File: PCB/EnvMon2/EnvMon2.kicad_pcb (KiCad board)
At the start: 2 copper layers, 57.5 x 37 mm, 38 parts, among them J1 USB-C, J2 DC, J3 TEMP, J4 Shelly, M1 OLED1.5-RGB, SW1 SW_Push, SW2 SW_Push, SW3 SW_Push, U1 LMR16006XDDCR, U2 SCD41, U3 FT231XQ, U4 ESP32-PICO-MINI-02, U5 QR, U6 VEML3235SL_RA

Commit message: Tweak connectors
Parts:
- J2: footprint RevK:Molex_MiniSPOX_H2RA -> RevK:PTSM-HH-2-RA-W
- J3: footprint RevK:Molex_MiniSPOX_H3RA -> RevK:PTSM-HH-3-RA
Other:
- outline, holes or cut-outs redrawn

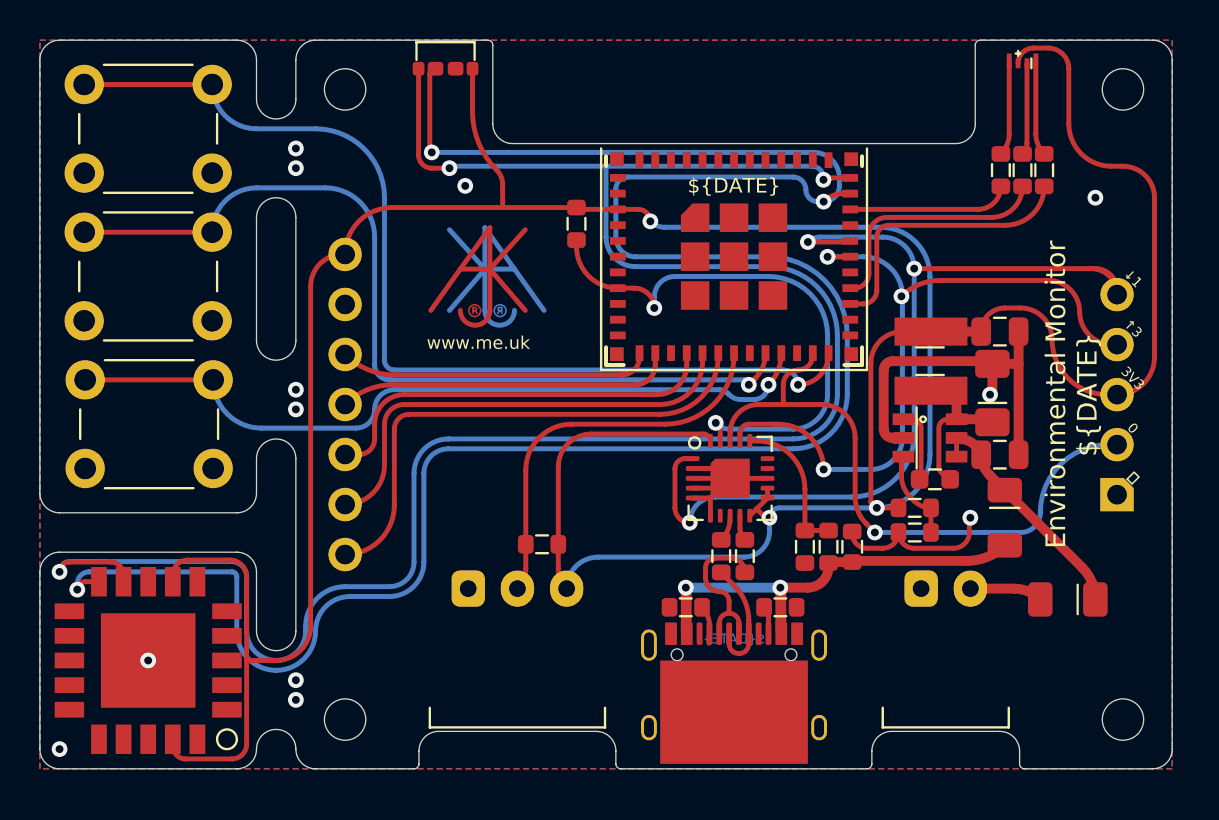
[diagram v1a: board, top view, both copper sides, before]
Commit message: New PCB with Sensitron SHT40 on board
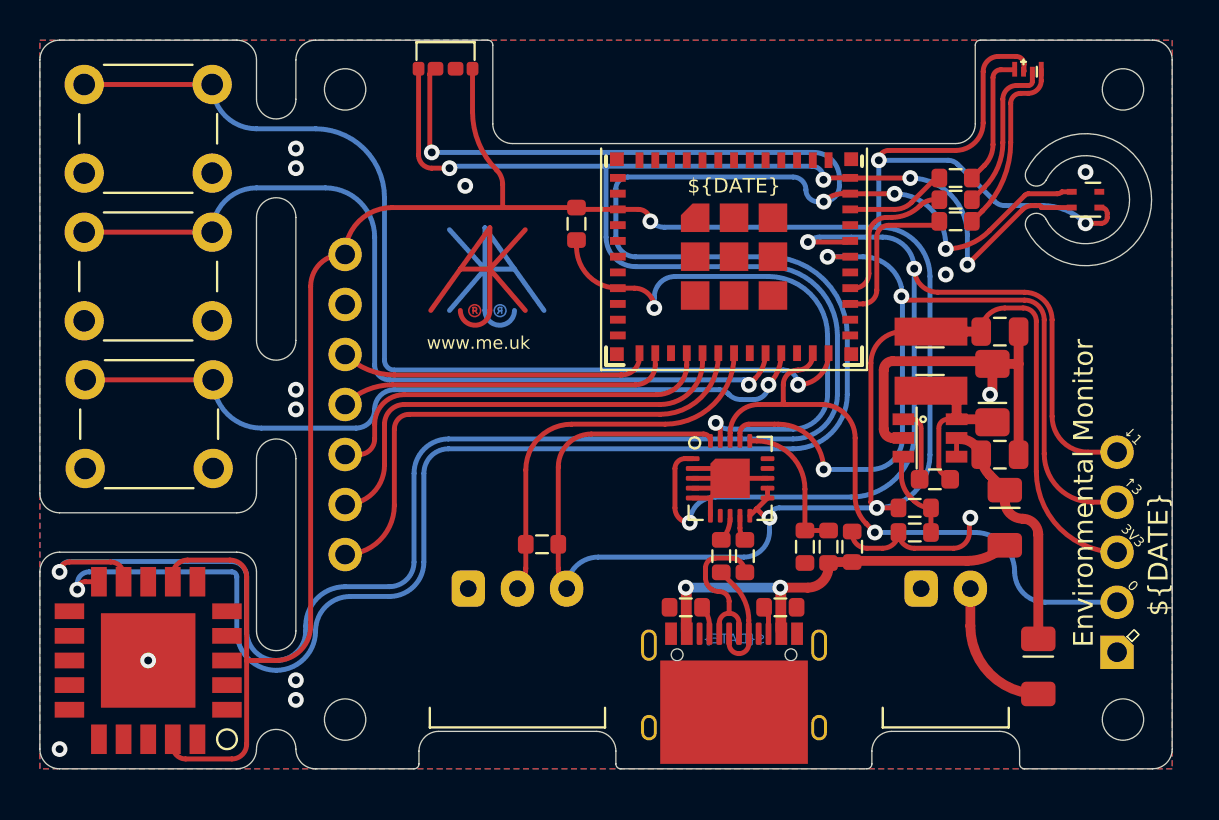
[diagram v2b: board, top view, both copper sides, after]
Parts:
- added U7: SHT40, RevK:Sensirion_DFN-4_1.5x1.5mm_P0.5mm_SHT4x, F.Cu at (140.1, 71.1)
- moved J4 8.00 mm to (141.7, 89.0)
- moved R8 5.20 mm to (133.5, 72.2), turned to 180 degrees
- moved R7 3.72 mm to (133.5, 71.1), turned to 180 degrees
- moved D4 3.72 mm to (137.7, 94.8), turned to -90 degrees
- moved R9 2.33 mm to (133.5, 70.0), turned to 180 degrees
- moved D3 0.51 mm to (137.2, 64.6)
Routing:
- net SCL: track 105.2 -> 120.7 mm, vias 3 -> 5
- net SDA: track 114.8 -> 128.7 mm, vias 3 -> 5
- net +3.3V: track 174.8 -> 188.4 mm, vias 3 -> 5
- net I: track 36.8 -> 43.9 mm
- net G: track 14.3 -> 7.85 mm
- net R: track 12.2 -> 7.12 mm
- net O: track 47.5 -> 52.4 mm
- net Net-(D3-Pad4): track 4.83 -> 9.31 mm
- net Net-(D4-Pad2): track 3.69 -> 7.18 mm
- net Net-(D3-Pad3): track 4.66 -> 8.07 mm
- net B: track 8.27 -> 5.11 mm
- net Net-(D3-Pad1): track 4.83 -> 6.80 mm
- net DC: track 10.5 -> 11.6 mm
- net GND: vias 12 -> 13
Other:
- outline, holes or cut-outs redrawn
- board text added: "H/T"

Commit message: Started EnvHT
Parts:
- added C5: 100nF, RevK:C_0603, F.Cu at (138.2, 66.5)
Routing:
- net +3.3V: track 188.4 -> 193.2 mm, vias 5 -> 6

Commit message: Silk and change VEML
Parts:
- removed U6: VEML3235SL_RA, RevK:VEML3235SL-RA
- added U8: VEML6040, RevK:VEML6040, F.Cu at (107.6, 64.1)
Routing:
- net SDA: track 128.6 -> 132.0 mm
- net SCL: track 120.7 -> 119.1 mm
- net I: track 43.9 -> 45.1 mm
- net +3.3V: track 193.2 -> 194.4 mm
- net GND: vias 13 -> 14
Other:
- board text added: "${CURRENT_DATE}"
- board text added: "8/7/19"
- board text removed: "${DATE}"
- board text removed: "LED: 8/7/19"

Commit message: SIlk
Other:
- board text added: "CLK"
- board text added: "CS"
- board text added: "DC"
- board text added: "DC 4V-40V 2W"
- board text added: "DIN"
- board text added: "RST"
- board text added: "SCD41"
- board text added: "SCL: 21 SDA: 22 RGB: 8/7/19"
- board text added: "SHT40"
- board text added: "VEML6040"
- board text removed: "8/7/19"
- board text removed: "DC 4V-60V"
- board text removed: "H/T"
- board text removed: "SCD41 SCL: 21 SDA: 22"
